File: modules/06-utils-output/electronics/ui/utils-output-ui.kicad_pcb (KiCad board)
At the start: 2 copper layers, 58 x 110 mm, 39 parts, among them J1 Conn_02x03_Odd_Even, J2 Conn_02x04_Odd_Even, J3 Conn_01x01_Pin, J4 Conn_01x02, J5 Conn_01x06, J6 Conn_02x05_Odd_Even, J7 Conn_02x03_Odd_Even, J8 Conn_01x01_Pin, Q1 2N3904, Q2 2N3906

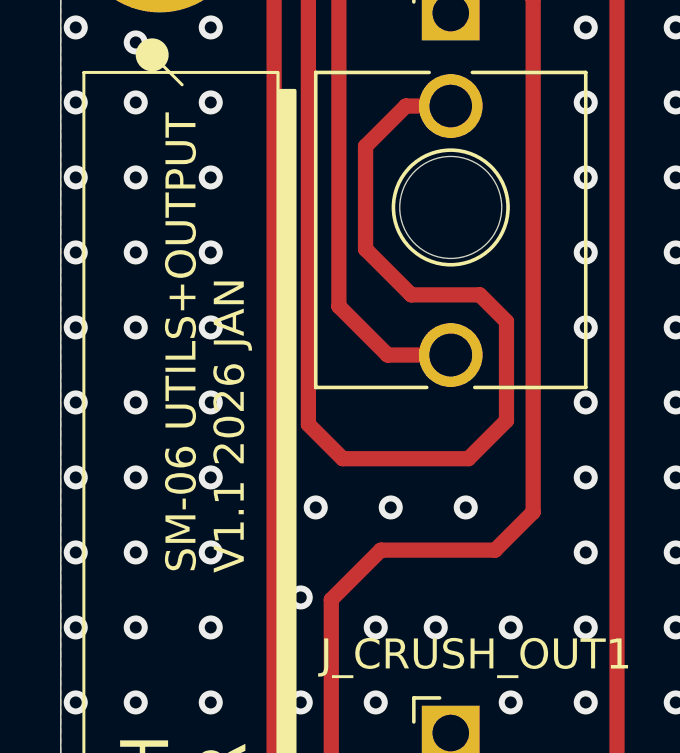
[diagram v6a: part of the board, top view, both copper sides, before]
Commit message: KiCAD version update - Utils
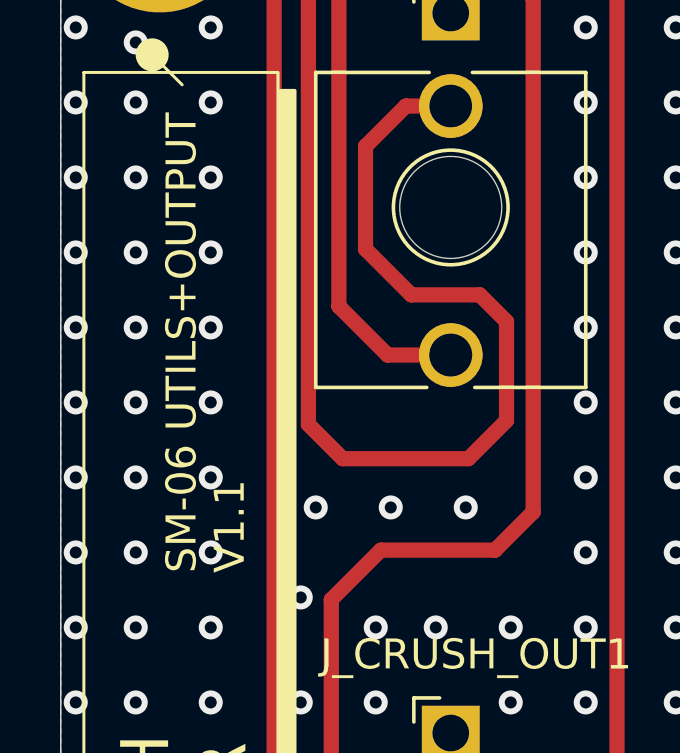
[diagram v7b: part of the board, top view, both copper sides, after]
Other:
- board text added: "SM-06 UTILS+OUTPUT V1.1"
- board text removed: "SM-06 UTILS+OUTPUT V1.1 2026 JAN"
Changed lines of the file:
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@@
 		)
 	)
-	(gr_text "SM-06 UTILS+OUTPUT\nV1.1 2026 JAN"
+	(gr_text "SM-06 UTILS+OUTPUT\nV1.1"
 		(at 130.223 127.185 90)
 		(layer "F.SilkS")
@@
 			(justify left bottom)
 		)
-		(render_cache "SM-06 UTILS+OUTPUT\nV1.1 2026 JAN" 90
+		(render_cache "SM-06 UTILS+OUTPUT\nV1.1" 90
 			(polygon
 				(pts
@@
 				)
 			)
-			(polygon
-				(pts
-					(xy 129.798498 122.607644) (xy 130.053 122.607644) (xy 130.053 121.97127) (xy 129.925749 121.97127)
-					(xy 129.925749 122.480394) (xy 129.798498 122.480394)
-				)
-			)
-			(polygon
-				(pts
-					(xy 129.162124 122.098581) (xy 129.034812 122.098581) (xy 129.034812 122.480394) (xy 129.162124 122.480394)
-				)
-			)
-			(polygon
-				(pts
-					(xy 129.162124 122.098581) (xy 129.416686 122.098581) (xy 129.416686 121.97127) (xy 129.162124 121.97127)
-				)
-			)
-			(polygon
-				(pts
-					(xy 129.671187 122.480394) (xy 129.798498 122.480394) (xy 129.798498 122.353082) (xy 129.671187 122.353082)
-				)
-			)
-			(polygon
-				(pts
-					(xy 129.162124 122.607644) (xy 129.289374 122.607644) (xy 129.289374 122.480394) (xy 129.162124 122.480394)
-				)
-			)
-			(polygon
-				(pts
-					(xy 129.416686 122.225832) (xy 129.543936 122.225832) (xy 129.543936 122.098581) (xy 129.416686 122.098581)
-				)
-			)
-			(polygon
-				(pts
-					(xy 129.543936 122.353082) (xy 129.671187 122.353082) (xy 129.671187 122.225832) (xy 129.543936 122.225832)
-				)
-			)
-			(polygon
-				(pts
-					(xy 129.162124 121.717623) (xy 129.925749 121.717623) (xy 129.925749 121.590373) (xy 129.671187 121.590373)
-					(xy 129.671187 121.463061) (xy 129.543936 121.463061) (xy 129.543936 121.590373) (xy 129.162124 121.590373)
-				)
-			)
-			(polygon
-				(pts
-					(xy 129.925749 121.590373) (xy 130.053 121.590373) (xy 130.053 121.20856) (xy 129.925749 121.20856)
-				)
-			)
-			(polygon
-				(pts
-					(xy 129.034812 121.590373) (xy 129.162124 121.590373) (xy 129.162124 121.20856) (xy 129.034812 121.20856)
-				)
-			)
-			(polygon
-				(pts
-					(xy 129.162124 121.20856) (xy 129.289374 121.20856) (xy 129.289374 121.335811) (xy 129.416686 121.335811)
-					(xy 129.416686 121.20856) (xy 129.925749 121.20856) (xy 129.925749 121.081249) (xy 129.162124 121.081249)
-				)
-			)
-			(polygon
-				(pts
-					(xy 129.416686 121.463061) (xy 129.543936 121.463061) (xy 129.543936 121.335811) (xy 129.416686 121.335811)
-				)
-			)
-			(polygon
-				(pts
-					(xy 129.798498 120.827602) (xy 130.053 120.827602) (xy 130.053 120.191228) (xy 129.925749 120.191228)
-					(xy 129.925749 120.700352) (xy 129.798498 120.700352)
-				)
-			)
-			(polygon
-				(pts
-					(xy 129.162124 120.318539) (xy 129.034812 120.318539) (xy 129.034812 120.700352) (xy 129.162124 120.700352)
-				)
-			)
-			(polygon
-				(pts
-					(xy 129.162124 120.318539) (xy 129.416686 120.318539) (xy 129.416686 120.191228) (xy 129.162124 120.191228)
-				)
-			)
-			(polygon
-				(pts
-					(xy 129.671187 120.700352) (xy 129.798498 120.700352) (xy 129.798498 120.57304) (xy 129.671187 120.57304)
-				)
-			)
-			(polygon
-				(pts
-					(xy 129.162124 120.827602) (xy 129.289374 120.827602) (xy 129.289374 120.700352) (xy 129.162124 120.700352)
-				)
-			)
-			(polygon
-				(pts
-					(xy 129.416686 120.44579) (xy 129.543936 120.44579) (xy 129.543936 120.318539) (xy 129.416686 120.318539)
-				)
-			)
-			(polygon
-				(pts
-					(xy 129.543936 120.57304) (xy 129.671187 120.57304) (xy 129.671187 120.44579) (xy 129.543936 120.44579)
-				)
-			)
-			(polygon
-				(pts
-					(xy 129.034812 119.810331) (xy 129.162124 119.810331) (xy 129.162124 119.428518) (xy 129.034812 119.428518)
-				)
-			)
-			(polygon
-				(pts
-					(xy 129.162124 119.937581) (xy 129.925749 119.937581) (xy 129.925749 119.810331) (xy 129.543936 119.810331)
-					(xy 129.543936 119.428518) (xy 129.416686 119.428518) (xy 129.416686 119.810331) (xy 129.162124 119.810331)
-				)
-			)
-			(polygon
-				(pts
-					(xy 129.543936 119.428518) (xy 129.925749 119.428518) (xy 129.925749 119.301207) (xy 129.543936 119.301207)
-				)
-			)
-			(polygon
-				(pts
-					(xy 129.925749 119.810331) (xy 130.053 119.810331) (xy 130.053 119.428518) (xy 129.925749 119.428518)
-				)
-			)
-			(polygon
-				(pts
-					(xy 129.162124 119.428518) (xy 129.289374 119.428518) (xy 129.289374 119.301207) (xy 129.162124 119.301207)
-				)
-			)
-			(polygon
-				(pts
-					(xy 129.925749 118.030289) (xy 129.798498 118.030289) (xy 129.798498 118.15754) (xy 129.925749 118.15754)
-				)
-			)
-			(polygon
-				(pts
-					(xy 129.925749 118.030289) (xy 130.053 118.030289) (xy 130.053 117.648476) (xy 129.925749 117.648476)
-				)
-			)
-			(polygon
-				(pts
-					(xy 129.162124 117.648476) (xy 129.925749 117.648476) (xy 129.925749 117.521165) (xy 129.034812 117.521165)
-					(xy 129.034812 117.902978) (xy 129.162124 117.902978)
-				)
-			)
-			(polygon
-				(pts
-					(xy 129.289374 117.267519) (xy 130.053 117.267519) (xy 130.053 117.140268) (xy 129.671187 117.140268)
-					(xy 129.671187 116.758456) (xy 130.053 116.758456) (xy 130.053 116.631144) (xy 129.289374 116.631144)
-					(xy 129.289374 116.758456) (xy 129.543936 116.758456) (xy 129.543936 117.140268) (xy 129.289374 117.140268)
-				)
-			)
-			(polygon
-				(pts
-					(xy 129.034812 117.012957) (xy 129.162124 117.012957) (xy 129.162124 116.885706) (xy 129.034812 116.885706)
-				)
-			)
-			(polygon
-				(pts
-					(xy 129.162124 117.140268) (xy 129.289374 117.140268) (xy 129.289374 117.012957) (xy 129.162124 117.012957)
-				)
-			)
-			(polygon
-				(pts
-					(xy 129.162124 116.885706) (xy 129.289374 116.885706) (xy 129.289374 116.758456) (xy 129.162124 116.758456)
-				)
-			)
-			(polygon
-				(pts
-					(xy 129.034812 116.377498) (xy 130.053 116.377498) (xy 130.053 116.250247) (xy 129.416686 116.250247)
-					(xy 129.416686 116.122936) (xy 129.289374 116.122936) (xy 129.289374 116.250247) (xy 129.034812 116.250247)
-				)
-			)
-			(polygon
-				(pts
-					(xy 129.671187 115.868435) (xy 130.053 115.868435) (xy 130.053 115.741123) (xy 129.034812 115.741123)
-					(xy 129.034812 115.868435) (xy 129.543936 115.868435) (xy 129.543936 115.995685) (xy 129.671187 115.995685)
-				)
-			)
-			(polygon
-				(pts
-					(xy 129.543936 115.995685) (xy 129.416686 115.995685) (xy 129.416686 116.122936) (xy 129.543936 116.122936)
-				)
-			)

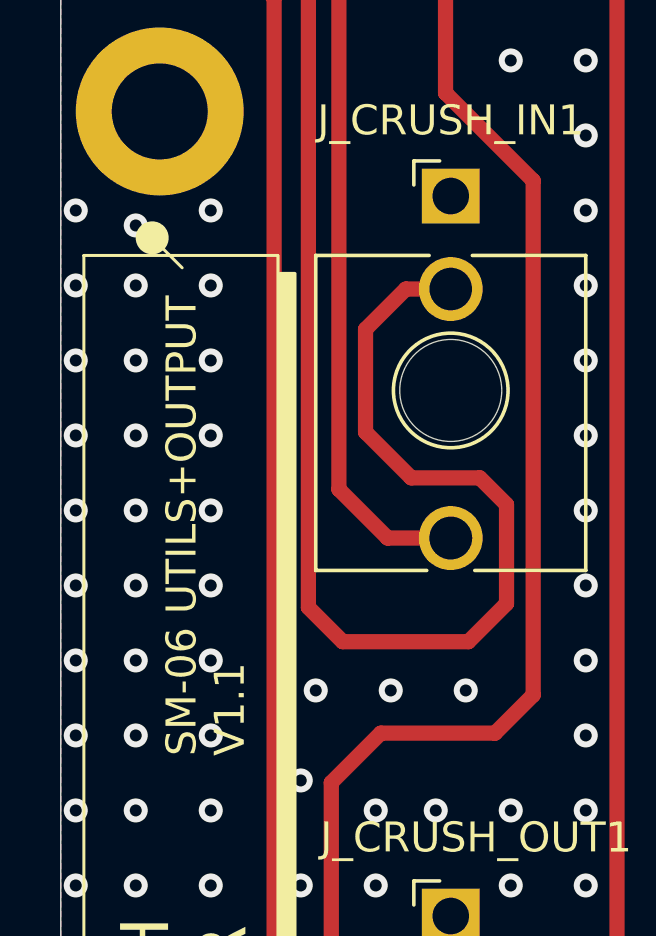
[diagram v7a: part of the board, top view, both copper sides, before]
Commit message: Changed board versioning to 'rev' on Utils
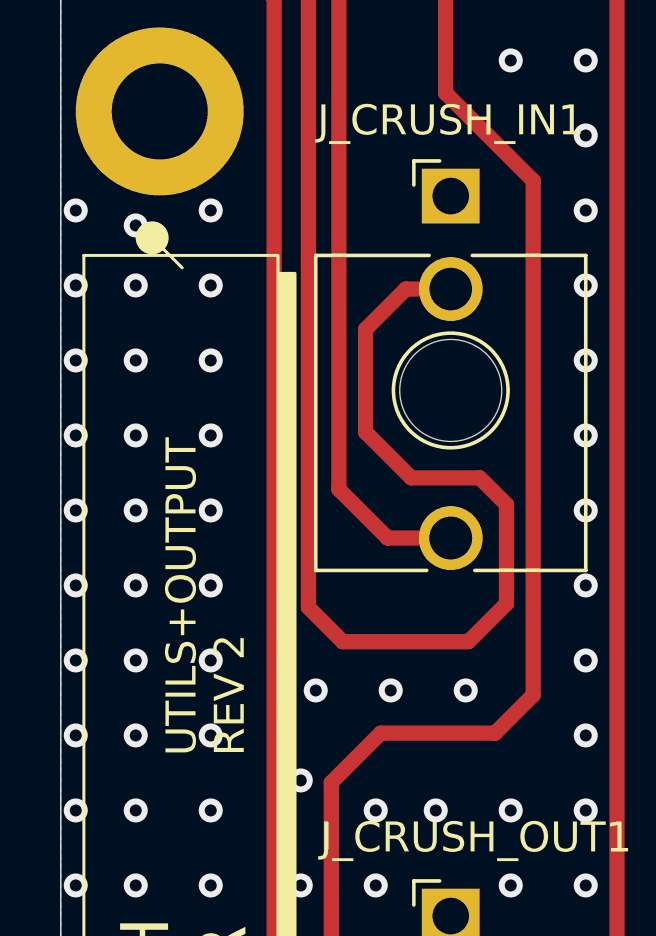
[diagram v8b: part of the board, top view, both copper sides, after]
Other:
- board text added: "UTILS+OUTPUT REV 2"
- board text removed: "SM-06 UTILS+OUTPUT V1.1"
